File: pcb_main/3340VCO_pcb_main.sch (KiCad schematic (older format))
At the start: 75 parts, among them J1 MJ-352, J2 MJ-352, J3 MJ-352, J4 POWER_IN, J5 MJ-352, J6 MJ-352, J7 MJ-352, U1 NJM074, U2 NJM074, U3 V3340M

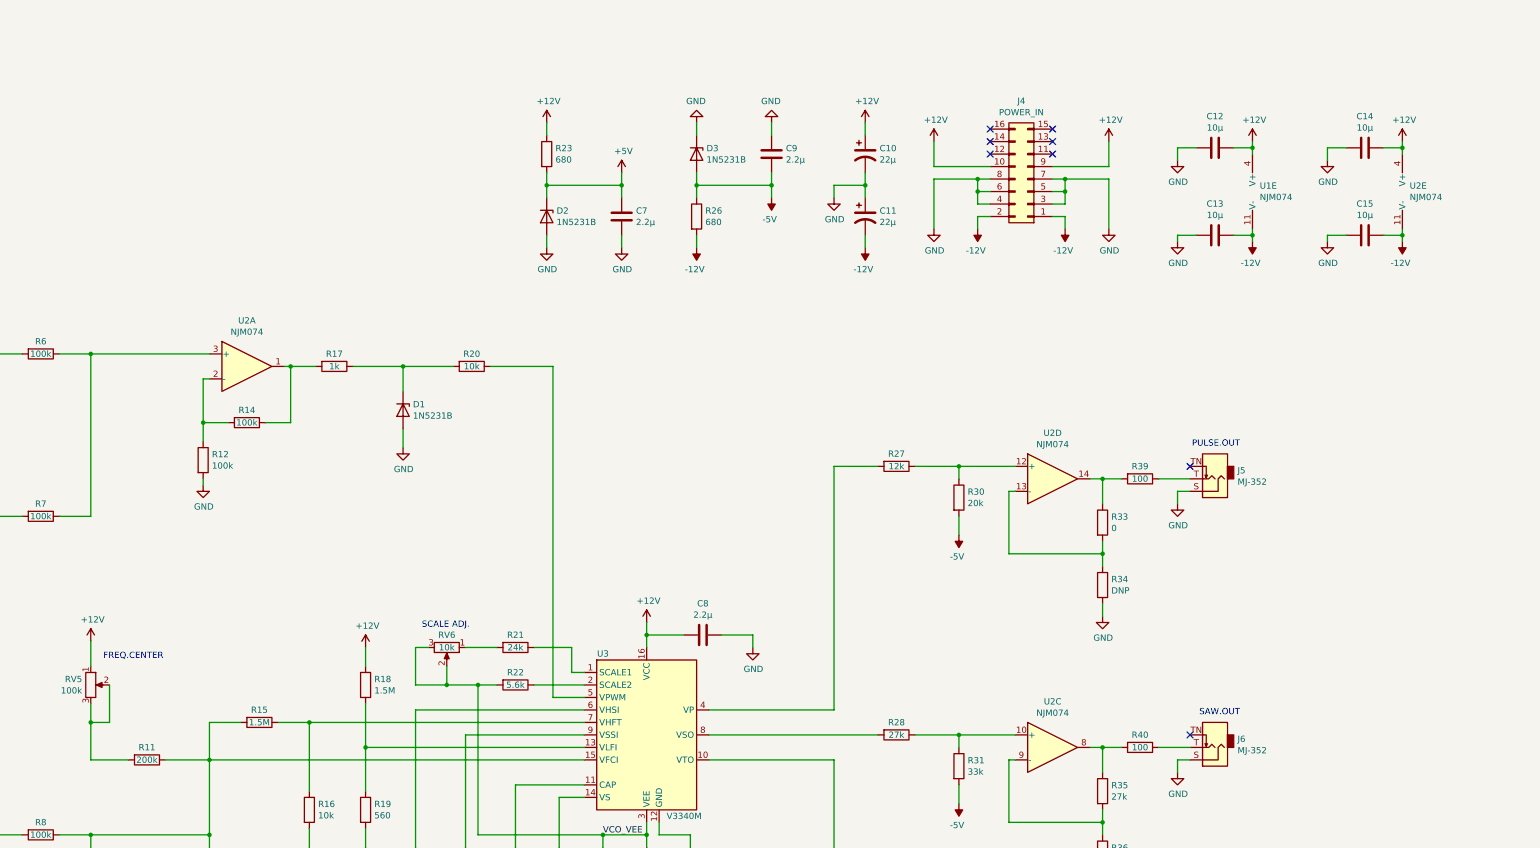
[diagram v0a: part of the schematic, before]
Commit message: flip RV5 pin assign, add power source protection diode
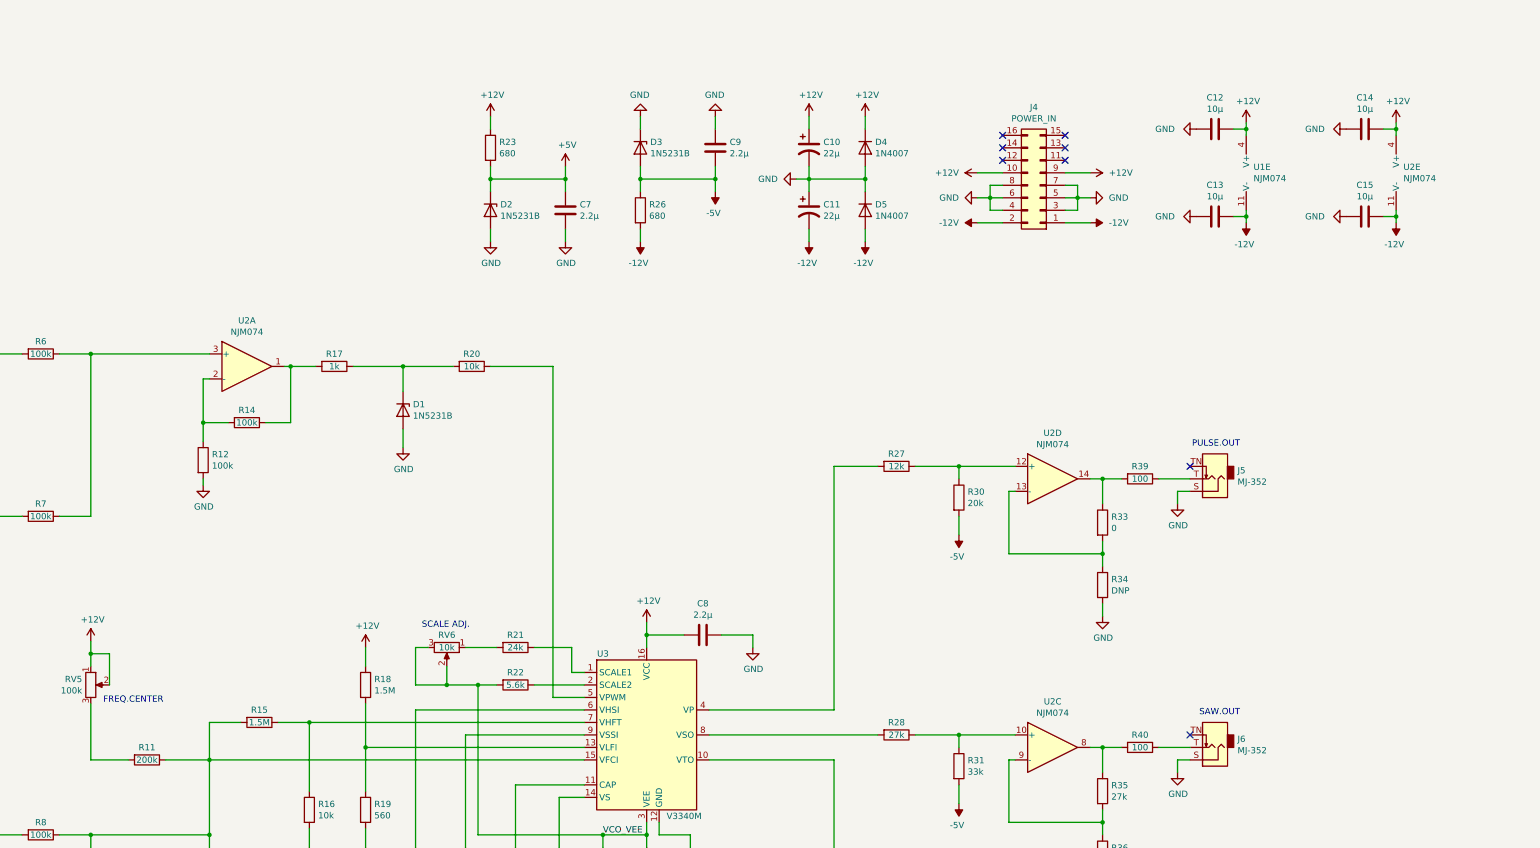
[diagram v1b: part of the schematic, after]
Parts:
- added D4, D5: 1N4007, Diode_THT:D_DO-41_SOD81_P10.16mm_Horizontal, symbol Diode:1N4007
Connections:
- net +12V: now also RV5.2, D4.1 (K)
- net -12V: now also D5.2 (A)
- net GND: now also D4.2 (A), D5.1 (K)
- net at R11.2, RV5.3: no longer RV5.2
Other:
- moved on the sheet: C10, C11, C12, C13, C14, C15, C7, C9, D2, D3, J4, R23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

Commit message: update schematic
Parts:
- removed D1: 1N5231B, Diode_THT:D_DO-34_SOD68_P10.16mm_Horizontal, symbol Device:D_Zener
- added R42: 27k, Resistor_THT:R_Axial_DIN0207_L6.3mm_D2.5mm_P2.54mm_Vertical, symbol Device:R
- D2, D3: footprint Diode_THT:D_DO-34_SOD68_P10.16mm_Horizontal -> Diode_THT:D_DO-34_SOD68_P2.54mm_Vertical_AnodeUp
- D4, D5: footprint Diode_THT:D_DO-41_SOD81_P10.16mm_Horizontal -> Diode_THT:D_DO-41_SOD81_P3.81mm_Vertical_AnodeUp
- J4: footprint Connector_PinHeader_2.54mm:PinHeader_2x08_P2.54mm_Vertical -> Connector_IDC:IDC-Header_2x08_P2.54mm_Horizontal
- R1, R10, R12, R13, R14, R15, R16, R18, R19, R2, R20, R21, R22, R23, R24, R26, R27, R28, R3, R30, R31, R32, R33, R34, R35, R36, R37, R38, R39, R4, R40, R41, R5, R6, R7, R8, R9: footprint Resistor_THT:R_Axial_DIN0207_L6.3mm_D2.5mm_P10.16mm_Horizontal -> Resistor_THT:R_Axial_DIN0207_L6.3mm_D2.5mm_P2.54mm_Vertical
- R11: value 200k -> 82k; footprint Resistor_THT:R_Axial_DIN0207_L6.3mm_D2.5mm_P10.16mm_Horizontal -> Resistor_THT:R_Axial_DIN0207_L6.3mm_D2.5mm_P2.54mm_Vertical
- R17: value 1k -> 1.5k; footprint Resistor_THT:R_Axial_DIN0207_L6.3mm_D2.5mm_P10.16mm_Horizontal -> Resistor_THT:R_Axial_DIN0207_L6.3mm_D2.5mm_P2.54mm_Vertical
- R25: value 820 -> 510; footprint Resistor_THT:R_Axial_DIN0207_L6.3mm_D2.5mm_P10.16mm_Horizontal -> Resistor_THT:R_Axial_DIN0207_L6.3mm_D2.5mm_P2.54mm_Vertical
- R29: value 39k -> 3.9k; footprint Resistor_THT:R_Axial_DIN0207_L6.3mm_D2.5mm_P10.16mm_Horizontal -> Resistor_THT:R_Axial_DIN0207_L6.3mm_D2.5mm_P2.54mm_Vertical
- RV5: value 100k -> 50k
- U3: footprint sop_conv:sop_conv_16pin -> Package_SO:SOIC-16_3.9x9.9mm_P1.27mm
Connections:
- net +12V: no longer RV5.1, RV5.2
- net +5V: now also RV5.1, RV5.2, R42.1; no longer RV1.3
- net GND: now also R17.2; no longer RV1.1
- net at R27.1, R30.1: now also U2.3 (+); no longer U2.12 (+)
- net at R5.1: now also U1.5 (+); no longer U1.3 (+)
- net at R33.1, R39.2: now also U2.1; no longer U2.14
- net at R17.1: now also RV1.1; no longer R20.2
- net at R2.1: now also U1.12 (+); no longer U1.10 (+)
- net at R3.1: now also U1.10 (+); no longer U1.12 (+)
- net at R12.1, R14.2: now also U2.13 (-); no longer U2.2 (-)
- net at R6.1, R7.1: now also U2.12 (+); no longer U2.3 (+)
- net at R33.2, R34.1: now also U2.2 (-); no longer U2.13 (-)
- net at R4.1: now also U1.3 (+); no longer U1.5 (+)
- net at R35.1, R40.2: now also U2.7; no longer U2.8
- net at R28.1, R31.1: now also U2.5 (+); no longer U2.10 (+)
- net at R35.2, R36.1: now also U2.6 (-); no longer U2.9 (-)
- net at R37.1, R41.2: now also U2.8; no longer U2.7
- net at R29.1, R32.1: now also U2.10 (+); no longer U2.5 (+)
- net at R37.2, R38.1: now also U2.9 (-); no longer U2.6 (-)
- net VCO_VEE renamed VEE
- new net: R42.2, RV1.3
- new net: R10.2, U1.6 (-), U1.7
- new net: R14.1, R20.2, U2.14
- new net: R6.2, U1.13 (-), U1.14
- new net: R7.2, U1.8, U1.9 (-)
- new net: R9.2, U1.1, U1.2 (-)
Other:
- note added: "-1.4 to 1.4V"
- note added: "-2.25 to 2.1V"
- note added: "-5.0 to 11.2V"
- note added: "-5.0 to 4.7V"
- note added: "-5.0 to 5.1V"
- note added: "-5.16 to 5.16V"
- note added: "0.0 to 3.9V"
- note added: "0.0 to 7.9V"
- moved on the sheet: C6, C7, D2, R23, R25

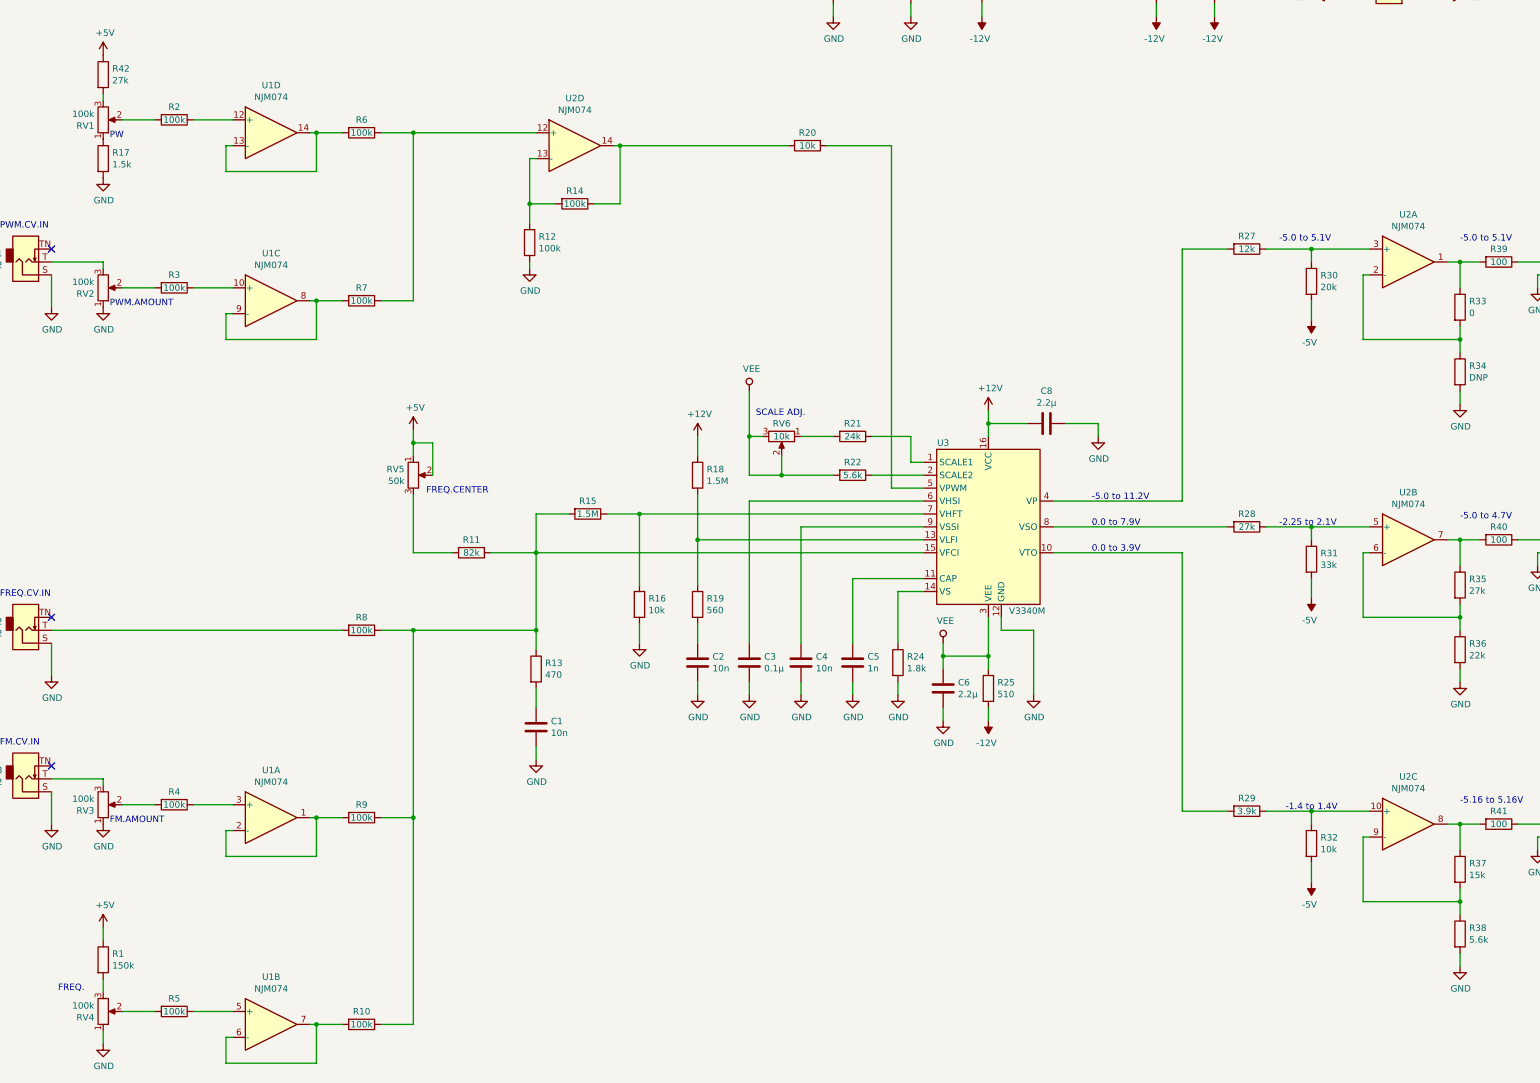
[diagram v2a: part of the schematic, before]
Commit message: redesign pcb_main for double-side
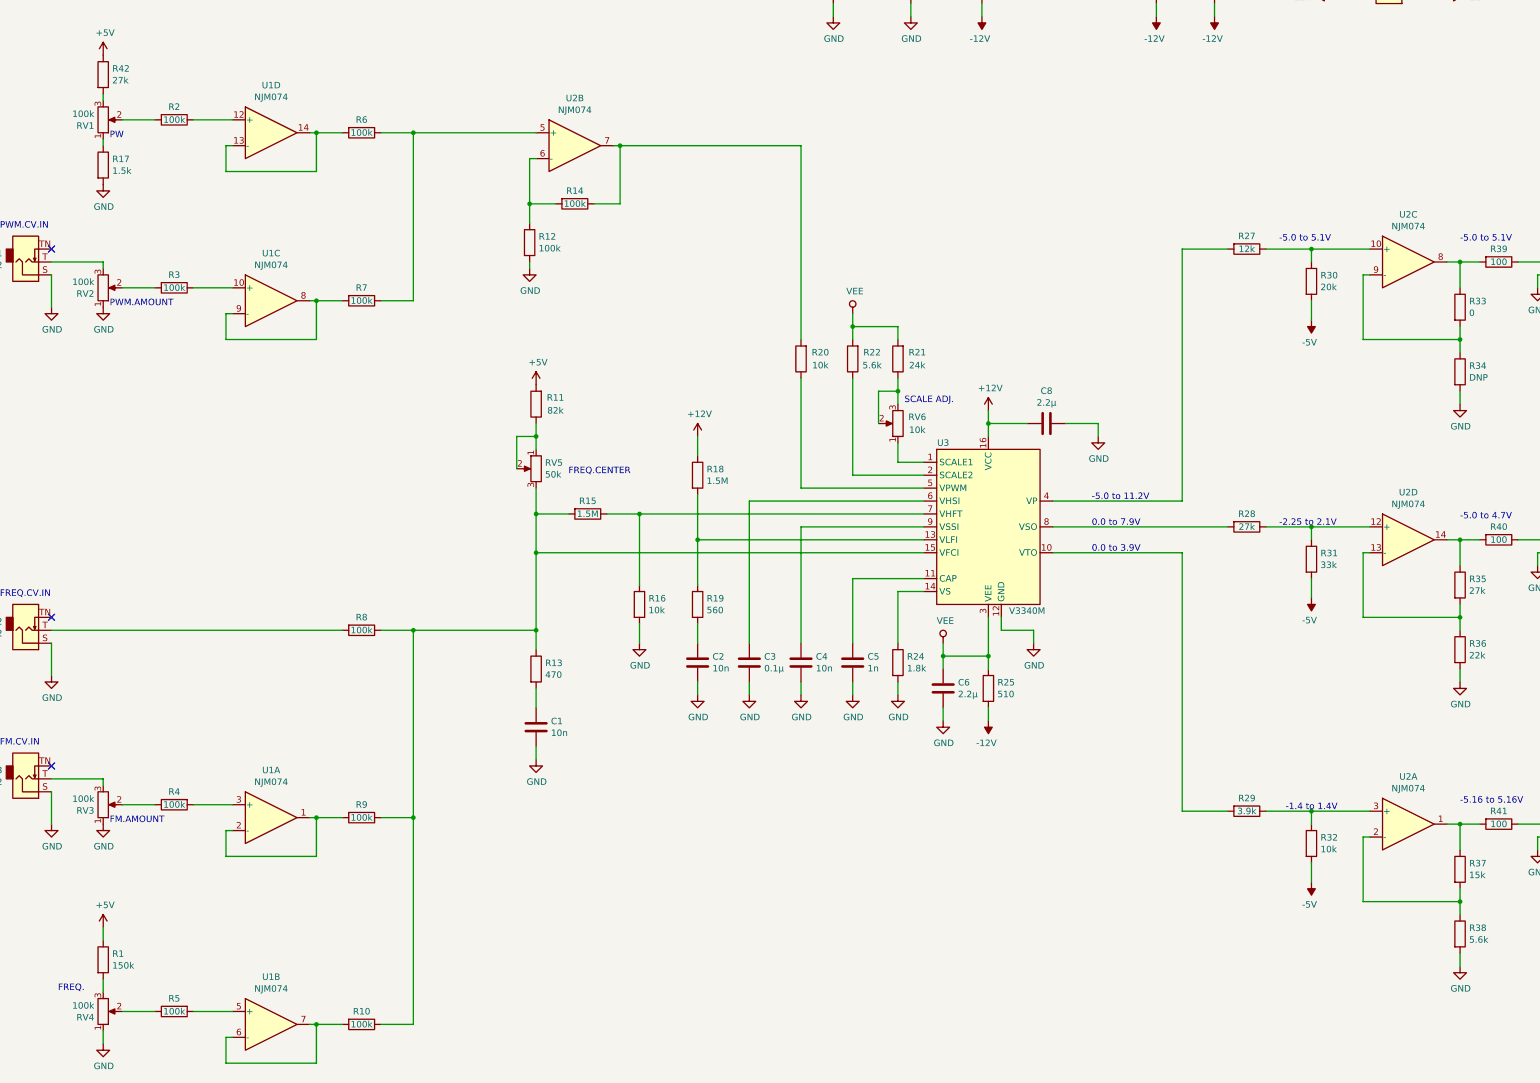
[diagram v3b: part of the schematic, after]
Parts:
- D2, D3: footprint Diode_THT:D_DO-34_SOD68_P2.54mm_Vertical_AnodeUp -> Diode_THT:D_DO-34_SOD68_P7.62mm_Horizontal
- R1, R11, R12, R17, R2, R20, R21, R23, R25, R26, R27, R28, R29, R3, R32, R38, R39, R42: footprint Resistor_THT:R_Axial_DIN0207_L6.3mm_D2.5mm_P2.54mm_Vertical -> Resistor_THT:R_Axial_DIN0207_L6.3mm_D2.5mm_P10.16mm_Horizontal
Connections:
- net +5V: now also R11.2; no longer RV5.1, RV5.2
- net VEE: now also R21.2; no longer RV6.2, RV6.3
- net at U3.1 (SCALE1): now also RV6.1; no longer R21.1
- net at R10.1, R13.1, R15.2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: now also RV5.3; no longer R11.1
- net at R27.1, R30.1: now also U2.10 (+); no longer U2.3 (+)
- net at RV4.2: now also R5.1; no longer R5.2
- net at U1.5 (+): now also R5.2; no longer R5.1
- net at R33.1, R39.2: now also U2.8; no longer U2.1
- net at R14.1, R20.2: now also U2.7; no longer U2.14
- net at R6.1, R7.1: now also U2.5 (+); no longer U2.12 (+)
- net at R12.1, R14.2: now also U2.6 (-); no longer U2.13 (-)
- net at R33.2, R34.1: now also U2.9 (-); no longer U2.2 (-)
- net at R4.1: now also RV3.2; no longer U1.3 (+)
- net at R4.2: now also U1.3 (+); no longer RV3.2
- net at R35.1, R40.2: now also U2.14; no longer U2.7
- net at R28.1, R31.1: now also U2.12 (+); no longer U2.5 (+)
- net at R35.2, R36.1: now also U2.13 (-); no longer U2.6 (-)
- net at R37.1, R41.2: now also U2.1; no longer U2.8
- net at R29.1, R32.1: now also U2.3 (+); no longer U2.10 (+)
- net at R37.2, R38.1: now also U2.2 (-); no longer U2.9 (-)
- new net: R21.1, RV6.2, RV6.3
- new net: R11.1, RV5.1, RV5.2
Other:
- moved on the sheet: R11, R17, R20, R21, R22, RV5, RV6
